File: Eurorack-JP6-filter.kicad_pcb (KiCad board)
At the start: 2 copper layers, 65 x 100 mm, 140 parts, among them J1 JACK_MONO_SW, J2 JACK_MONO_SW, J3 JACK_MONO_SW, J4 JACK_MONO_SW, J5 JACK_MONO_SW, J6 JACK_MONO_SW, P1 CONN_02X05, Q1 BCM857BS, Q2 BCM857BS, Q3 J112, Q4 J112, Q5 J112, Q6 J112, SW1 KS-01Q, U1 TL072-, U10 CD4027, U11 CD40106, U2 TL072-, U3 TL072-, U4 TL072-, U5 LM13700, U6 LM13700, U7 LM13700, U8 DG409, U9 CD4052

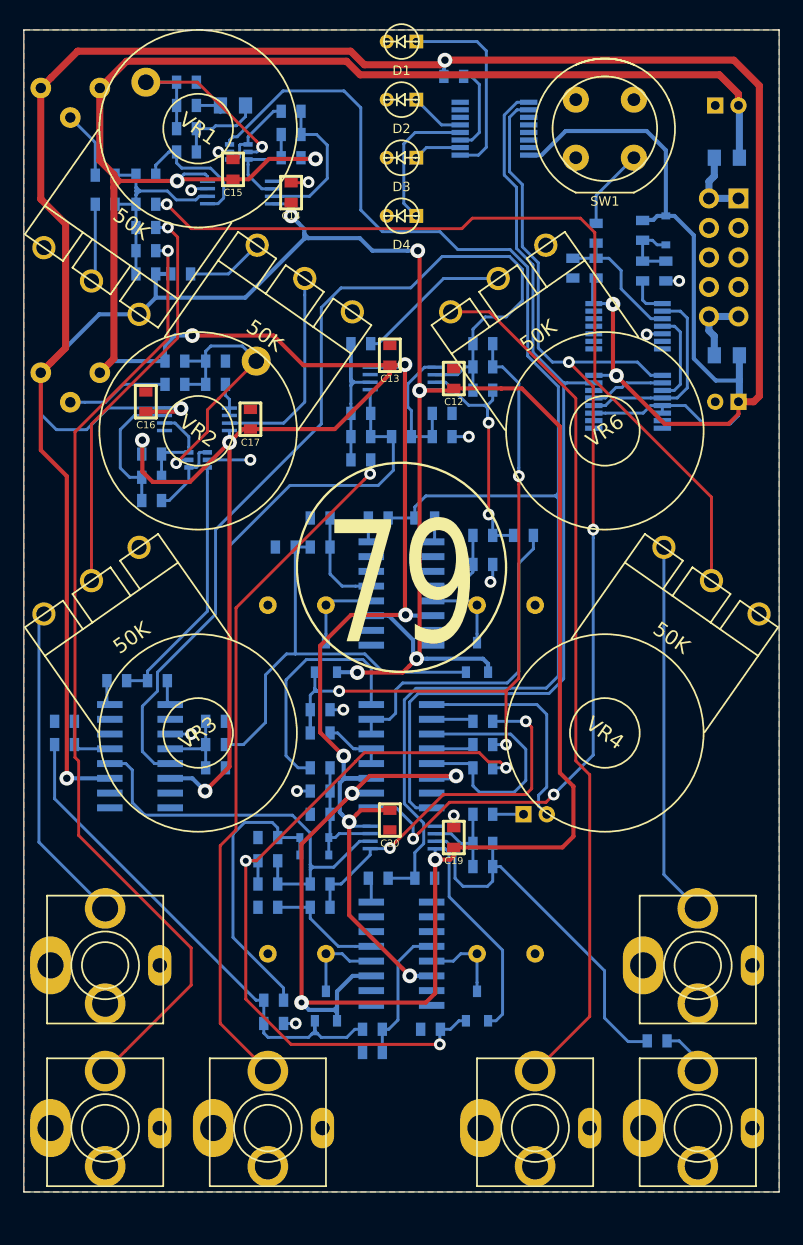
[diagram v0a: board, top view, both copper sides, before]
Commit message: JFET buffer 33K R to GND error fixed to -12V
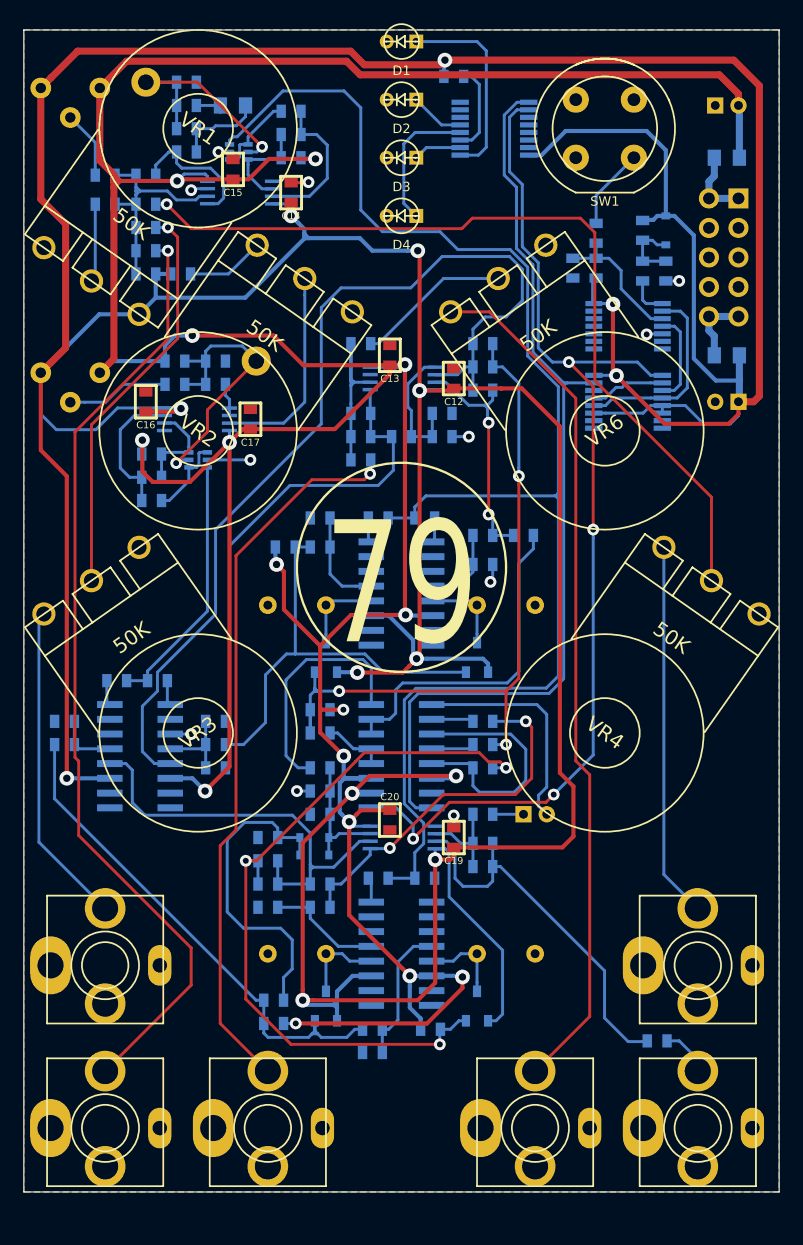
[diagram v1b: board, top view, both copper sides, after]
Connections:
- R33 pad 1: GND -> -12V
- R40 pad 1: GND -> -12V
- R57 pad 1: GND -> -12V
- R69 pad 1: GND -> -12V
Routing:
- net -12V: track 287.4 -> 326.3 mm, vias 11 -> 15
- net Net-(D5-Pad2): track 24.8 -> 27.7 mm
- net Net-(J5-Pad3): track 59.7 -> 62.3 mm
- net GND: track 19.8 -> 17.3 mm, vias 13 -> 11
- net +12V: track 519.8 -> 518.5 mm
- net Net-(R48-Pad1): track 31.9 -> 31.4 mm
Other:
- board text added: "Multimode Filter v1.1 07 2015"
- board text removed: "Multimode Filter v1.0 05 2015"

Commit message: Power polarity protection diodes added, TSSOP-8 footprints changed to KiCad standard, removal of references to VRML1 models, Gerber plots updated
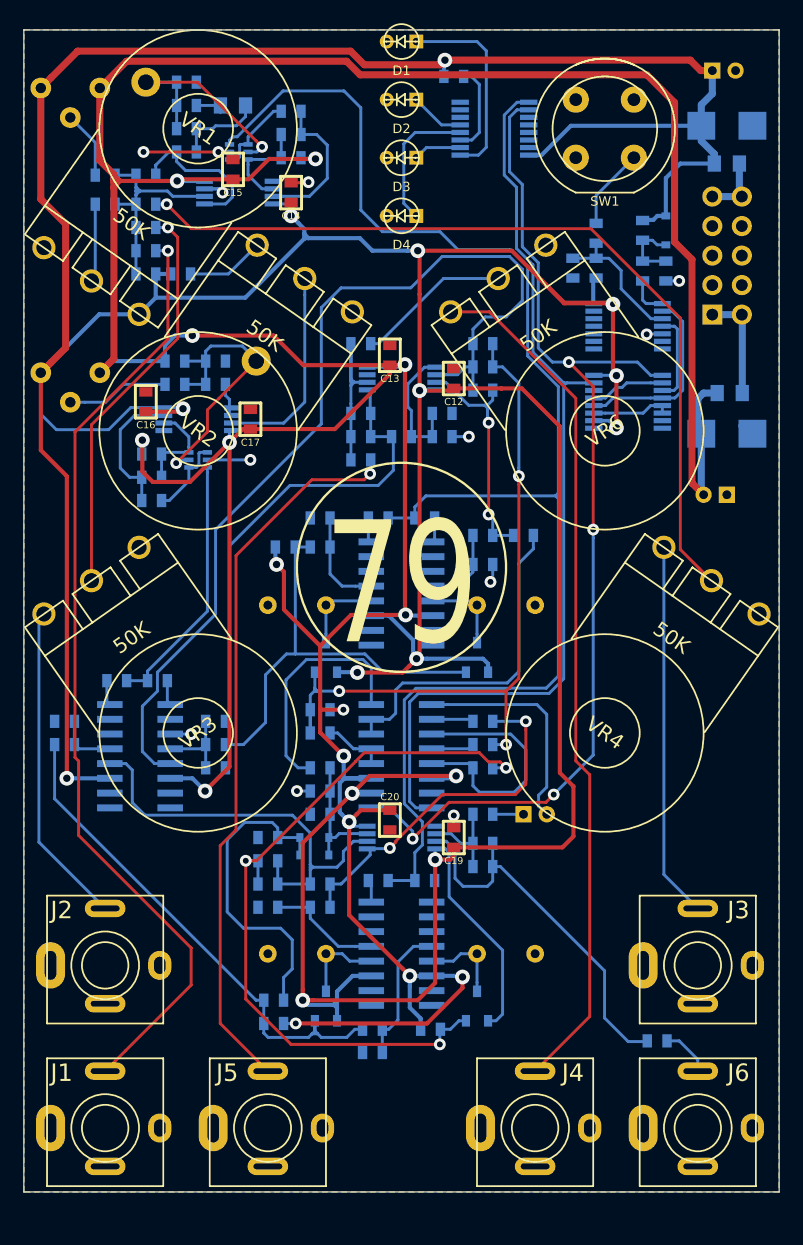
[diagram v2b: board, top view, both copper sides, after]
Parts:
- added D8: S1BB, MyModules:SMB-1C2A, B.Cu at (72.5, 20.2)
- added D9: S1BB, MyModules:SMB-1C2A, B.Cu at (72.5, 46.8)
- J1, J2, J3, J4, J5, J6: footprint MyModules:PJ-301B-JACK -> MyModules:PJ-301B-JACK-SLOTS
- R61: value 33K -> 100K
- U1, U2, U3, U4: footprint MyModules:TSSOP8-JRL -> MyModules:TSSOP-8_4.4x3mm_Pitch0.65mm
- moved C24 33.5 mm to (71.5, 52.0), turned to 180 degrees
- moved C23 28.5 mm to (72.2, 15.5), turned to 0 degrees
- moved R67 20.3 mm to (72.8, 43.2), turned to 0 degrees
- moved R66 16.5 mm to (72.5, 23.5), turned to 0 degrees
- moved P1 10.2 mm to (71.2, 36.5), turned to 0 degrees
- moved R56 0.20 mm to (42.5, 85.2)
- moved R68 0.20 mm to (46.5, 85.2)
- turned U1 to 0 degrees
- turned U2 to 180 degrees
- turned U3 to 0 degrees
- turned U4 to 0 degrees
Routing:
- net +12V: track 518.5 -> 484.4 mm, vias 14 -> 15
- net -12V: track 326.3 -> 359.7 mm
- net GND: track 17.3 -> 24.8 mm, vias 11 -> 12
- net Net-(P1-Pad1): track 6.23 -> 9.42 mm
- net Net-(R13-Pad1): track 11.8 -> 13.5 mm
- net Net-(U10-Pad12): track 17.1 -> 16.2 mm
- net Net-(R4-Pad2): track 73.7 -> 72.9 mm
- net Net-(P1-Pad10): track 6.18 -> 5.47 mm
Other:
- board text added: "Multimode Filter v1.2 05 2016"
- board text removed: "Multimode Filter v1.1 07 2015"

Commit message: schematic edited, changes simulated. ready to change layout
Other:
- board text added: "Multimode Filter v1.3 10 2016"
- board text removed: "Multimode Filter v1.2 05 2016"
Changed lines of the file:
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@@
     (links 317)
     (no_connects 0)
-    (area 8.999999 -2.400001 80.000001 126.300001)
+    (area 11.949999 11.949999 77.050001 112.050001)
     (thickness 1.6)
     (drawings 34)
@@
     (effects (font (size 1.5 1.5) (thickness 0.3)) (justify mirror))
   )
-  (gr_text "Multimode Filter\nv1.2 05 2016\n" (at 67 83.25) (layer B.SilkS)
+  (gr_text "Multimode Filter\nv1.3 10 2016\n" (at 67 83.25) (layer B.SilkS)
     (effects (font (size 1.5 1.5) (thickness 0.3)) (justify mirror))
   )

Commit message: hacking together v1.3 pcb
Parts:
- removed system79-logo-12mm: VAL**, synth:system79-logo-12mm
- removed system79-logo-18mm: VAL**, synth:system79-logo-18mm
- added C26: 100n, MyModules:SM0603-C-JRL, F.Cu at (42.9, 109.1)
- added C27: 100n, MyModules:SM0603-C-JRL, F.Cu at (44.2, 105.6)
- added D10: 1N914, MyModules:SOD323-C1A2, F.Cu at (40.4, 104.7)
- added R73: 100K, MyModules:SM0603-R-JRL, B.Cu at (28.0, 52.5)
- added R74: 100K, MyModules:SM0603-R-JRL, B.Cu at (17.8, 53.2)
- added R75: 100K, MyModules:SM0603-R-JRL, F.Cu at (46.7, 109.7)
- added R76: 47K, MyModules:SM0603-R-JRL, F.Cu at (38.7, 109.7)
- added R77: 100K, MyModules:SM0603-R-JRL, F.Cu at (47.4, 104.5)
- added R78: 100K, MyModules:SM0603-R-JRL, F.Cu at (33.5, 106.1)
- added U12: TS321, TO_SOT_Packages_SMD:SOT-23-5, B.Cu at (21.8, 62.2)
- added U13: TS321, TO_SOT_Packages_SMD:SOT-23-5, B.Cu at (30.5, 25.5)
- added VR8: 100K, MyModules:TC33X-2, B.Cu at (24.5, 100.0)
- C10, C23, C24: footprint MyModules:2MM-POL-CAP -> Capacitors_SMD:c_elec_5x5.3
- C12, C13, C16, C17, C19, C20: moved to B.Cu
- J1, J2, J3, J4, J5, J6: footprint MyModules:PJ-301B-JACK-SLOTS -> MyModules:PJ-301B-JACK
- U1, U2, U3, U4: footprint MyModules:TSSOP-8_4.4x3mm_Pitch0.65mm -> MyModules:TSSOP8-JRL
- VR5, VR7: footprint MyModules:Bourns_3362P -> MyModules:TC33X-2
- moved R4 29.6 mm to (17.8, 56.2), turned to 270 degrees
- moved R2 19.1 mm to (28.0, 49.2), turned to 90 degrees
- moved Q1 17.1 mm to (21.8, 65.2)
- moved U1 12.0 mm to (37.3, 16.1), turned to 90 degrees
- moved C17 11.9 mm to (26.0, 56.0), turned to 90 degrees
- moved R27 11.2 mm to (28.8, 28.2)
- moved R20 10.9 mm to (25.0, 63.2), turned to 90 degrees
- moved R21 10.8 mm to (21.8, 59.2)
- moved C2 8.98 mm to (25.0, 59.2), turned to 90 degrees
- moved C20 8.49 mm to (37.5, 74.0), turned to 0 degrees
- moved U2 8.39 mm to (23.2, 53.0), turned to 270 degrees
- moved R12 8.05 mm to (25.0, 47.8)
- moved R9 8.05 mm to (25.0, 49.8)
- moved R11 7.95 mm to (21.8, 49.8)
- moved R15 7.95 mm to (21.8, 47.8)
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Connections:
- J1 pad 2: Net-(J1-Pad2) -> (no net)
- J2 pad 2: Net-(J2-Pad2) -> (no net)
- J3 pad 2: Net-(J3-Pad2) -> (no net)
- J4 pad 2: Net-(J4-Pad2) -> (no net)
- J5 pad 2: Net-(J5-Pad2) -> (no net)
- J6 pad 2: Net-(J6-Pad2) -> (no net)
- R2 pad 1: Net-(R10-Pad1) -> Net-(R2-Pad1)
- R2 pad 2: Net-(J1-Pad3) -> Net-(R2-Pad2)
- R4 pad 1: Net-(R10-Pad1) -> Net-(D10-Pad1)
- R4 pad 2: Net-(R4-Pad2) -> Net-(J1-Pad3)
- R9 pad 2: Net-(R9-Pad2) -> Net-(R73-Pad1)
- U1 pad 5: GND -> Net-(U1-Pad5)
- U1 pad 6: Net-(C5-Pad2) -> Net-(R77-Pad2)
- U1 pad 7: Net-(C5-Pad1) -> Net-(R77-Pad1)
- U10 pad 14: Net-(U10-Pad14) -> (no net)
- U11 pad 10: Net-(U11-Pad10) -> (no net)
- U11 pad 12: Net-(U11-Pad12) -> (no net)
- U11 pad 6: Net-(U11-Pad6) -> (no net)
- U11 pad 8: Net-(U11-Pad8) -> (no net)
- U2 pad 1: Net-(R9-Pad2) -> Net-(R73-Pad1)
- U2 pad 2: Net-(R9-Pad2) -> Net-(R2-Pad1)
- U2 pad 3: Net-(U2-Pad3) -> GND
- U2 pad 6: Net-(C2-Pad2) -> Net-(D10-Pad1)
- U2 pad 7: Net-(C2-Pad1) -> Net-(D10-Pad2)
- U5 pad 15: Net-(U5-Pad15) -> (no net)
- U5 pad 2: Net-(U5-Pad2) -> (no net)
- U6 pad 15: Net-(U6-Pad15) -> (no net)
- U6 pad 2: Net-(U6-Pad2) -> (no net)
- U7 pad 15: Net-(U7-Pad15) -> (no net)
- U7 pad 2: Net-(U7-Pad2) -> (no net)
- U9 pad 11: Net-(U9-Pad11) -> (no net)
- U9 pad 12: Net-(U9-Pad12) -> (no net)
- U9 pad 14: Net-(U9-Pad14) -> (no net)
- U9 pad 15: Net-(U9-Pad15) -> (no net)
- VR2 pad 1: GND -> Net-(R1-Pad2)
- VR2 pad 2: Net-(U2-Pad3) -> Net-(R2-Pad2)
- VR2 pad 3: Net-(R1-Pad2) -> GND
- VR4 pad 2: Net-(R4-Pad2) -> Net-(U1-Pad5)
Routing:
- net Net-(U1-Pad5): track 0.00 -> 72.9 mm, vias 0 -> 1
- net Net-(R4-Pad2): track 72.9 -> 0.00 mm, vias 1 -> 0
- net -12V: track 359.7 -> 321.4 mm
- net Net-(J1-Pad3): track 82.2 -> 47.0 mm
- net Net-(Q1-Pad5): track 24.4 -> 1.80 mm, vias 1 -> 0
- net Net-(R2-Pad2): track 0.00 -> 21.6 mm
- net RES_CTRL: track 22.3 -> 1.80 mm
- net +12V: track 484.4 -> 466.6 mm, vias 15 -> 16
- net Net-(U2-Pad3): track 17.9 -> 0.00 mm
- net Net-(C2-Pad1): track 11.8 -> 0.00 mm
- net Net-(R13-Pad1): track 13.5 -> 3.30 mm
- net Net-(C5-Pad1): track 12.9 -> 3.68 mm
- net Net-(R11-Pad2): track 8.79 -> 0.00 mm
- net Net-(C2-Pad2): track 8.34 -> 0.00 mm
- net Net-(R2-Pad1): track 0.00 -> 7.98 mm
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
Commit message: v1.3 routed
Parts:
- C14, C15, C26, C27, D10, R75, R76, R77, R78: moved to B.Cu
- J1, J2, J3, J4, J5, J6: footprint MyModules:PJ-301B-JACK -> MyModules:PJ-301B-JACK-SLOTS
- Q1, Q2: footprint MyModules:SOT363-JRL -> SMD TRAN:sot323-6
- moved C26 92.4 mm to (22.5, 19.0), turned to 180 degrees
- moved R76 91.1 mm to (14.0, 22.0), turned to 270 degrees
- moved R78 87.4 mm to (26.0, 19.0), turned to 180 degrees
- moved R77 86.9 mm to (21.0, 21.8), turned to 270 degrees
- moved C27 82.0 mm to (29.0, 25.0), turned to 90 degrees
- moved VR8 79.6 mm to (17.5, 20.8), turned to 180 degrees
- moved R75 63.4 mm to (24.0, 50.5)
- moved D10 57.2 mm to (15.5, 53.2), turned to 270 degrees
- moved R1 17.1 mm to (42.5, 34.8), turned to 270 degrees
- moved R10 16.4 mm to (26.0, 17.0), turned to 180 degrees
- moved C14 12.9 mm to (44.5, 34.8), turned to 270 degrees
- moved R27 12.9 mm to (41.2, 25.2), turned to 90 degrees
- moved U1 12.4 mm to (26.2, 21.8), turned to 270 degrees
- moved C5 11.6 mm to (41.2, 21.0), turned to 90 degrees
- moved VR5 11.1 mm to (17.8, 28.0), turned to 180 degrees
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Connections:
- J1 pad 2: (no net) -> Net-(J1-Pad2)
- J2 pad 2: (no net) -> Net-(J2-Pad2)
- J3 pad 2: (no net) -> Net-(J3-Pad2)
- J4 pad 2: (no net) -> Net-(J4-Pad2)
- J5 pad 2: (no net) -> Net-(J5-Pad2)
- J6 pad 2: (no net) -> Net-(J6-Pad2)
- R76 pad 2: Net-(J3-Pad3) -> Net-(J2-Pad3)
- U10 pad 14: (no net) -> Net-(U10-Pad14)
- U11 pad 10: (no net) -> Net-(U11-Pad10)
- U11 pad 12: (no net) -> Net-(U11-Pad12)
- U11 pad 6: (no net) -> Net-(U11-Pad6)
- U11 pad 8: (no net) -> Net-(U11-Pad8)
- U5 pad 15: (no net) -> Net-(U5-Pad15)
- U5 pad 2: (no net) -> Net-(U5-Pad2)
- U6 pad 15: (no net) -> Net-(U6-Pad15)
- U6 pad 2: (no net) -> Net-(U6-Pad2)
- U7 pad 15: (no net) -> Net-(U7-Pad15)
- U7 pad 2: (no net) -> Net-(U7-Pad2)
- U9 pad 11: (no net) -> Net-(U9-Pad11)
- U9 pad 12: (no net) -> Net-(U9-Pad12)
- U9 pad 14: (no net) -> Net-(U9-Pad14)
- U9 pad 15: (no net) -> Net-(U9-Pad15)
- VR3 pad 2: Net-(R3-Pad2) -> Net-(U1-Pad5)
- VR4 pad 2: Net-(U1-Pad5) -> Net-(R3-Pad2)
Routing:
- net Net-(J2-Pad3): track 27.9 -> 68.4 mm
- net Net-(R3-Pad2): track 34.9 -> 72.1 mm
- net Net-(Q1-Pad5): track 1.80 -> 38.1 mm
- net Net-(U1-Pad5): track 72.9 -> 39.6 mm
- net +12V: track 466.6 -> 497.6 mm, vias 16 -> 21
- net FREQ_CTRL: track 118.8 -> 105.4 mm
- net Net-(C2-Pad2): track 0.00 -> 10.5 mm
- net GND: track 19.0 -> 28.7 mm, vias 7 -> 14
- net Net-(D10-Pad2): track 0.00 -> 9.39 mm
- net Net-(R77-Pad2): track 0.00 -> 8.76 mm
- net Net-(D10-Pad1): track 0.00 -> 6.64 mm
- net Net-(R77-Pad1): track 0.00 -> 6.44 mm
- net Net-(Q1-Pad1): track 0.00 -> 6.38 mm
- net Net-(C2-Pad1): track 0.00 -> 6.15 mm
- net Net-(R13-Pad1): track 3.30 -> 7.61 mm
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
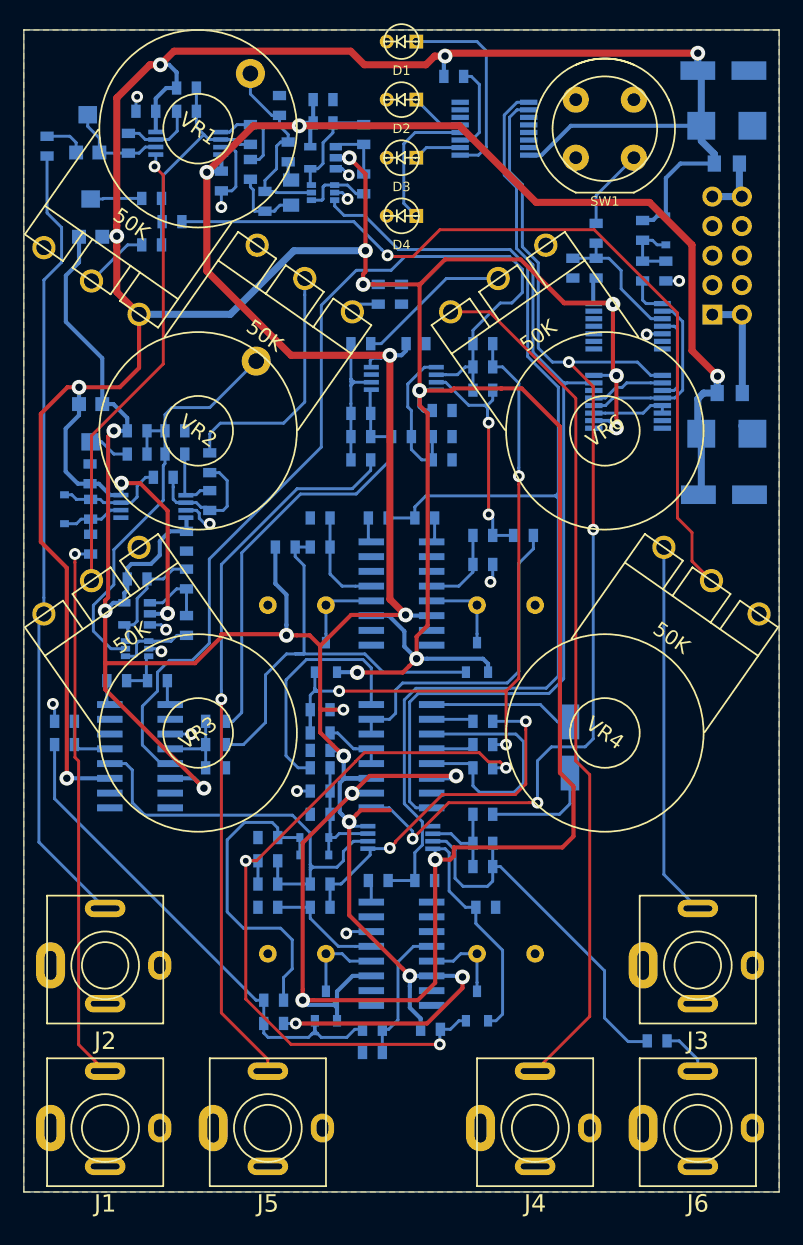
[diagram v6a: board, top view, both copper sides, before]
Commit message: routed and DRC passed, silkscreen edited
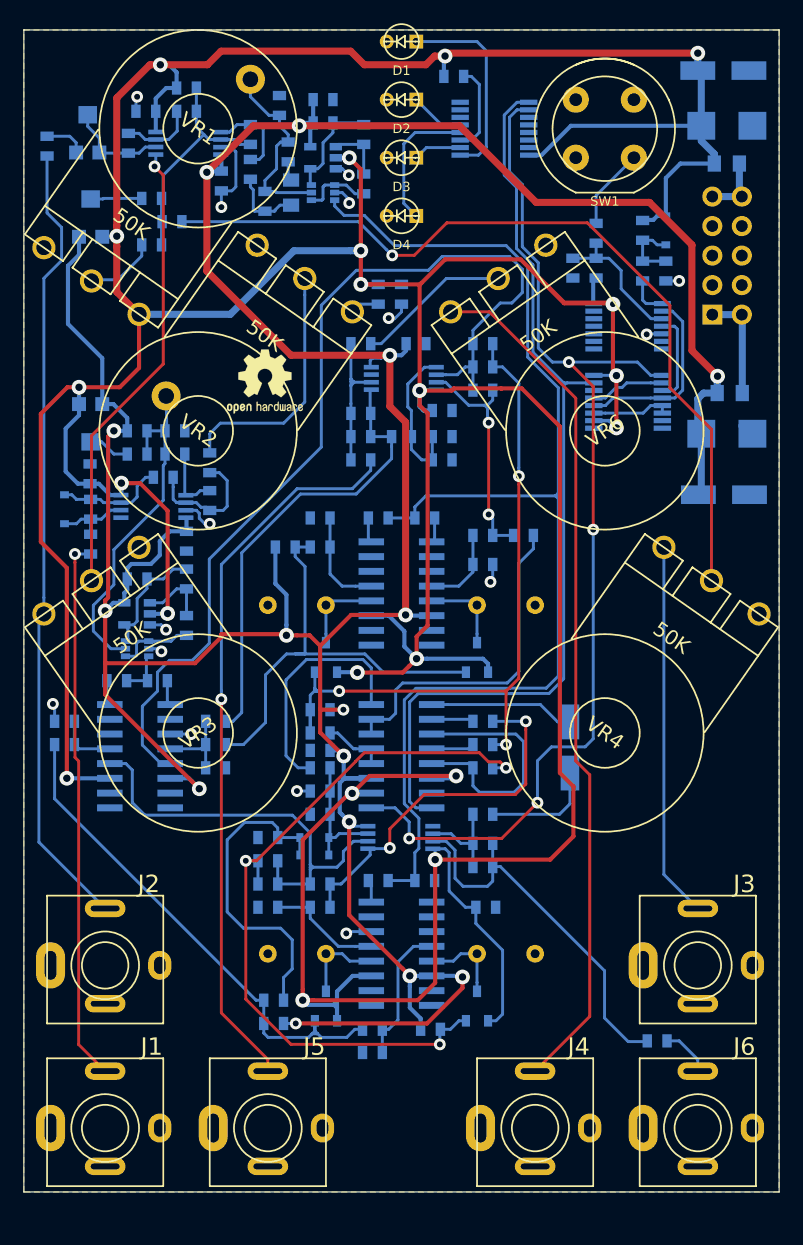
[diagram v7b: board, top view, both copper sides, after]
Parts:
- added REF***: OSHW-Logo2_7.3x6mm_SilkScreen, Symbols:OSHW-Logo2_7.3x6mm_SilkScreen, F.Cu at (32.8, 42.2)
- added REF***: OSHW-Symbol_6.7x6mm_SilkScreen, Symbols:OSHW-Symbol_6.7x6mm_SilkScreen, B.Cu at (44.2, 107.2)
- moved TP1 8.31 mm to (24.2, 43.5)
- moved TP2 0.50 mm to (31.5, 16.2)
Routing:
- net Net-(Q1-Pad5): track 38.1 -> 30.0 mm
- net -12V: track 320.3 -> 315.7 mm
- net GND: track 28.7 -> 31.1 mm, vias 14 -> 15
- net Net-(R48-Pad1): track 31.0 -> 31.9 mm
- net Net-(R5-Pad2): track 6.07 -> 6.63 mm
- net +12V: track 497.6 -> 497.0 mm
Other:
- board text added: "CENTRE"

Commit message: fixed cretnious things only a cretin would do
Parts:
- removed the REF*** at (32.8, 42.2)
- moved R1 12.9 mm to (30.0, 31.8)
- moved C14 6.05 mm to (39.2, 31.8)
- moved R7 2.46 mm to (40.0, 41.2), turned to 90 degrees
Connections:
- R1 pad 1: +12V -> Net-(R1-Pad1)
- R1 pad 2: Net-(R1-Pad2) -> -12V
- VR2 pad 1: Net-(R1-Pad2) -> GND
- VR2 pad 3: GND -> Net-(R1-Pad1)
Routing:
- net +12V: track 497.0 -> 491.8 mm, vias 21 -> 20
- net Net-(C1-Pad2): track 12.5 -> 8.96 mm
- net Net-(R7-Pad2): track 13.3 -> 16.1 mm
- net Net-(R1-Pad2): track 2.50 -> 0.00 mm
- net -12V: track 315.7 -> 318.1 mm, vias 15 -> 16
- net Net-(R1-Pad1): track 0.00 -> 2.27 mm
- net GND: track 31.1 -> 31.7 mm
